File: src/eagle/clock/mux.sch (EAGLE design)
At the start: 52 parts, among them U1 SN74HC595N, U2 SN74HC595N, U3 SN74HC595N

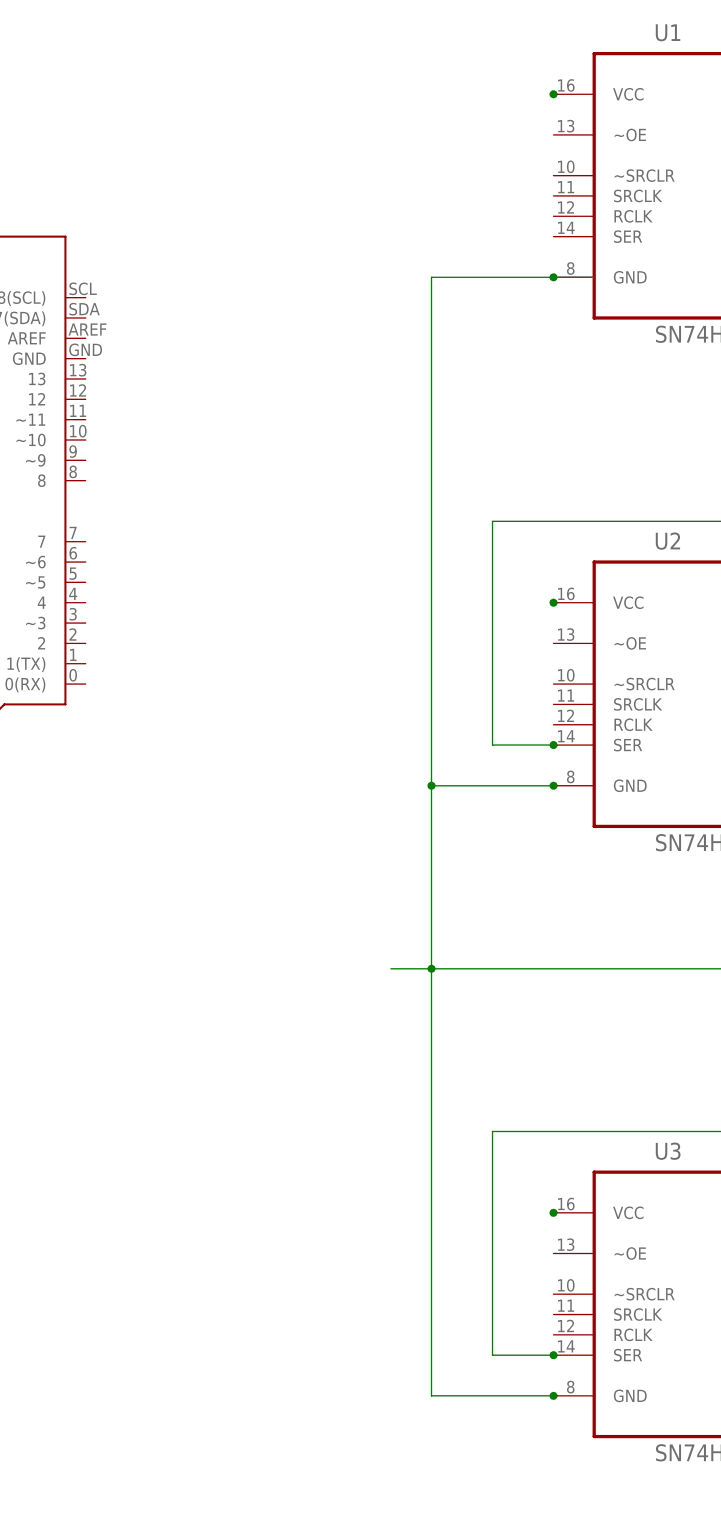
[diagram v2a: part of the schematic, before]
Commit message: Connect ~OE to GND
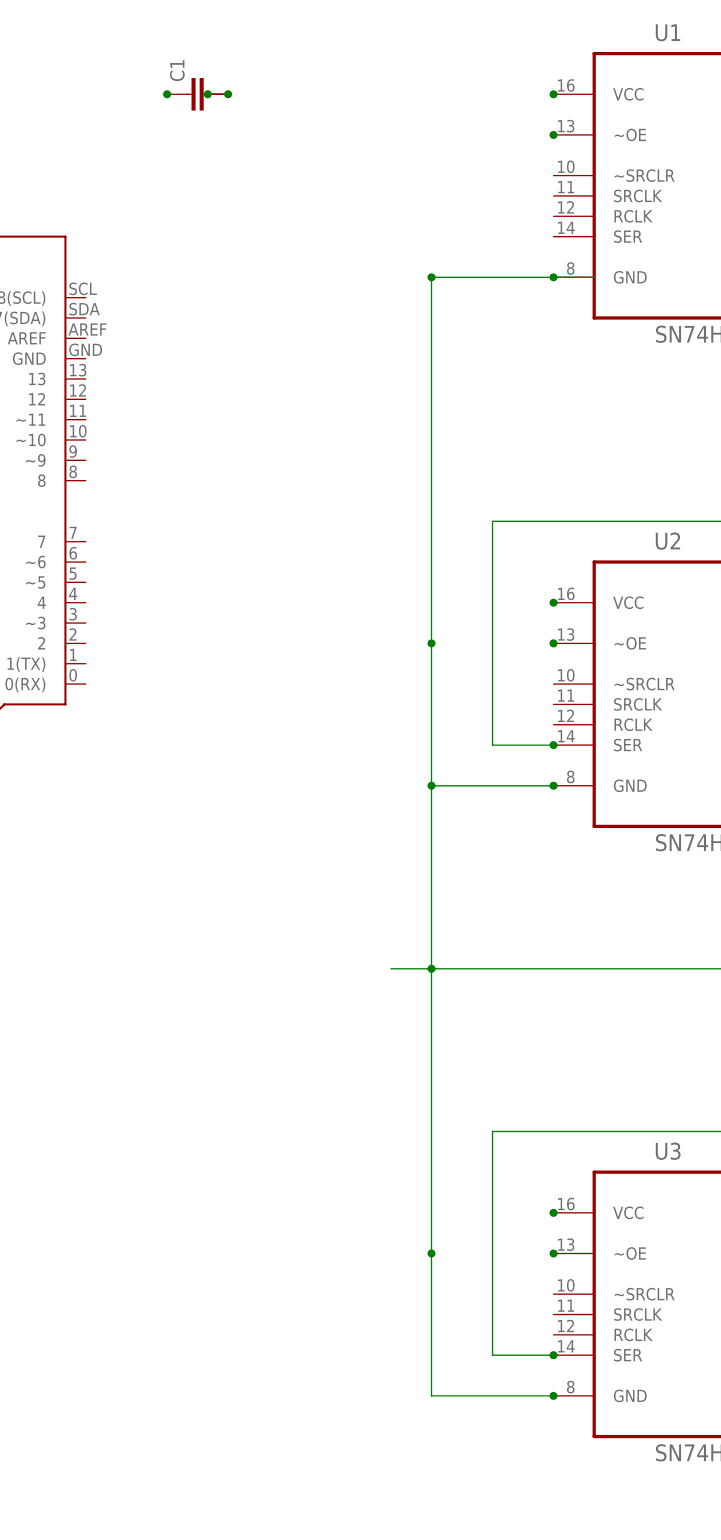
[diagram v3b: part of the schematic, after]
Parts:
- added C1: (no value), capacitor-wima:C-10-15/6
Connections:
- new net N$50: C1.1
- new net N$51: C1.2
- new net N$59: C1.3
- new net N$60: U1.~OE
- new net N$61: U2.~OE
- new net N$62: U3.~OE
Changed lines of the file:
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@@
 <part name="U3" library="SN74HC595N" deviceset="SN74HC595N" device=""/>
 <part name="PCB1" library="E14_Arduino_published" deviceset="ARDUINO_UNO" device=""/>
+<part name="C1" library="capacitor-wima" deviceset="C-" device="10-15/6"/>
 </parts>
 <sheets>
@@
 <plain>
 <wire x1="20.32" y1="60.96" x2="-7.62" y2="60.96" width="0.1524" layer="93"/>
-<wire x1="-7.62" y1="60.96" x2="-116.84" y2="60.96" width="0.1524" layer="93"/>
 <wire x1="-7.62" y1="60.96" x2="-7.62" y2="-2.54" width="0.1524" layer="93"/>
 <wire x1="-7.62" y1="-2.54" x2="20.32" y2="-2.54" width="0.1524" layer="93"/>
@@
 <wire x1="-116.84" y1="60.96" x2="-116.84" y2="15.24" width="0.1524" layer="93"/>
 <wire x1="-116.84" y1="15.24" x2="-81.28" y2="15.24" width="0.1524" layer="93"/>
+<wire x1="-116.84" y1="60.96" x2="-7.62" y2="60.96" width="0.1524" layer="93"/>
+<wire x1="20.32" y1="55.88" x2="5.08" y2="55.88" width="0.1524" layer="93"/>
+<wire x1="5.08" y1="55.88" x2="5.08" y2="38.1" width="0.1524" layer="93"/>
+<wire x1="20.32" y1="-7.62" x2="5.08" y2="-7.62" width="0.1524" layer="93"/>
+<wire x1="20.32" y1="-83.82" x2="5.08" y2="-83.82" width="0.1524" layer="93"/>
 </plain>
 <instances>
@@
 <instance part="U3" gate="A" x="38.1" y="-86.36"/>
 <instance part="PCB1" gate="G$1" x="-58.42" y="12.7" rot="R270"/>
+<instance part="C1" gate="G$1" x="-25.4" y="60.96" rot="R90"/>
 </instances>
 <busses>
@@
 <wire x1="25.4" y1="38.1" x2="20.32" y2="38.1" width="0.1524" layer="91"/>
 <wire x1="20.32" y1="38.1" x2="5.08" y2="38.1" width="0.1524" layer="91"/>
-<wire x1="5.08" y1="38.1" x2="5.08" y2="-25.4" width="0.1524" layer="91"/>
+<wire x1="5.08" y1="38.1" x2="5.08" y2="-7.62" width="0.1524" layer="91"/>
 <pinref part="U2" gate="A" pin="GND"/>
+<wire x1="5.08" y1="-7.62" x2="5.08" y2="-25.4" width="0.1524" layer="91"/>
 <wire x1="5.08" y1="-25.4" x2="20.32" y2="-25.4" width="0.1524" layer="91"/>
 <wire x1="5.08" y1="-25.4" x2="5.08" y2="-48.26" width="0.1524" layer="91"/>
 <pinref part="U3" gate="A" pin="GND"/>
-<wire x1="5.08" y1="-48.26" x2="5.08" y2="-101.6" width="0.1524" layer="91"/>
+<wire x1="5.08" y1="-48.26" x2="5.08" y2="-83.82" width="0.1524" layer="91"/>
+<wire x1="5.08" y1="-83.82" x2="5.08" y2="-101.6" width="0.1524" layer="91"/>
 <wire x1="5.08" y1="-101.6" x2="20.32" y2="-101.6" width="0.1524" layer="91"/>
 <pinref part="U1" gate="A" pin="GND"/>
@@
 <junction x="5.08" y="-48.26"/>
 <junction x="5.08" y="-25.4"/>
+<junction x="5.08" y="-83.82"/>
+<junction x="5.08" y="-7.62"/>
+<junction x="5.08" y="38.1"/>
 </segment>
 </net>
@@
 </segment>
 </net>
+<net name="N$50" class="0">
+<segment>
+<pinref part="C1" gate="G$1" pin="1"/>
+<junction x="-27.94" y="60.96"/>
+</segment>
+</net>
+<net name="N$51" class="0">
+<segment>
+<pinref part="C1" gate="G$1" pin="2"/>
+<junction x="-20.32" y="60.96"/>
+</segment>
+</net>
+<net name="N$59" class="0">
+<segment>
+<pinref part="C1" gate="G$1" pin="3"/>
+<junction x="-22.86" y="60.96"/>
+</segment>
+</net>
+<net name="N$60" class="0">
+<segment>
+<pinref part="U1" gate="A" pin="~OE"/>
+<junction x="20.32" y="55.88"/>
+</segment>
+</net>
+<net name="N$61" class="0">
+<segment>
+<pinref part="U2" gate="A" pin="~OE"/>
+<junction x="20.32" y="-7.62"/>
+</segment>
+</net>
+<net name="N$62" class="0">
+<segment>
+<pinref part="U3" gate="A" pin="~OE"/>
+<junction x="20.32" y="-83.82"/>
+</segment>
+</net>

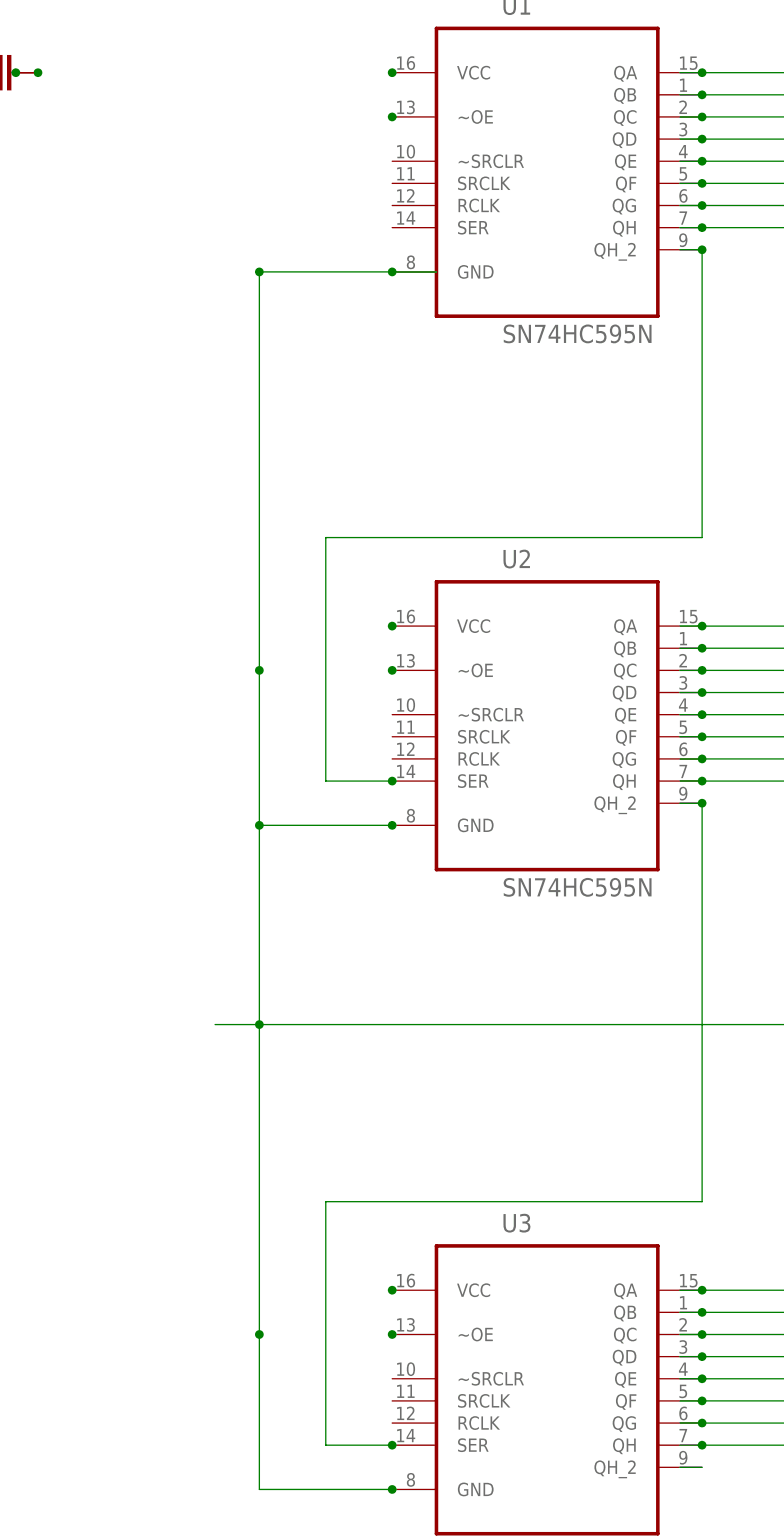
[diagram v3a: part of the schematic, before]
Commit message: 5V=>~SRCLR
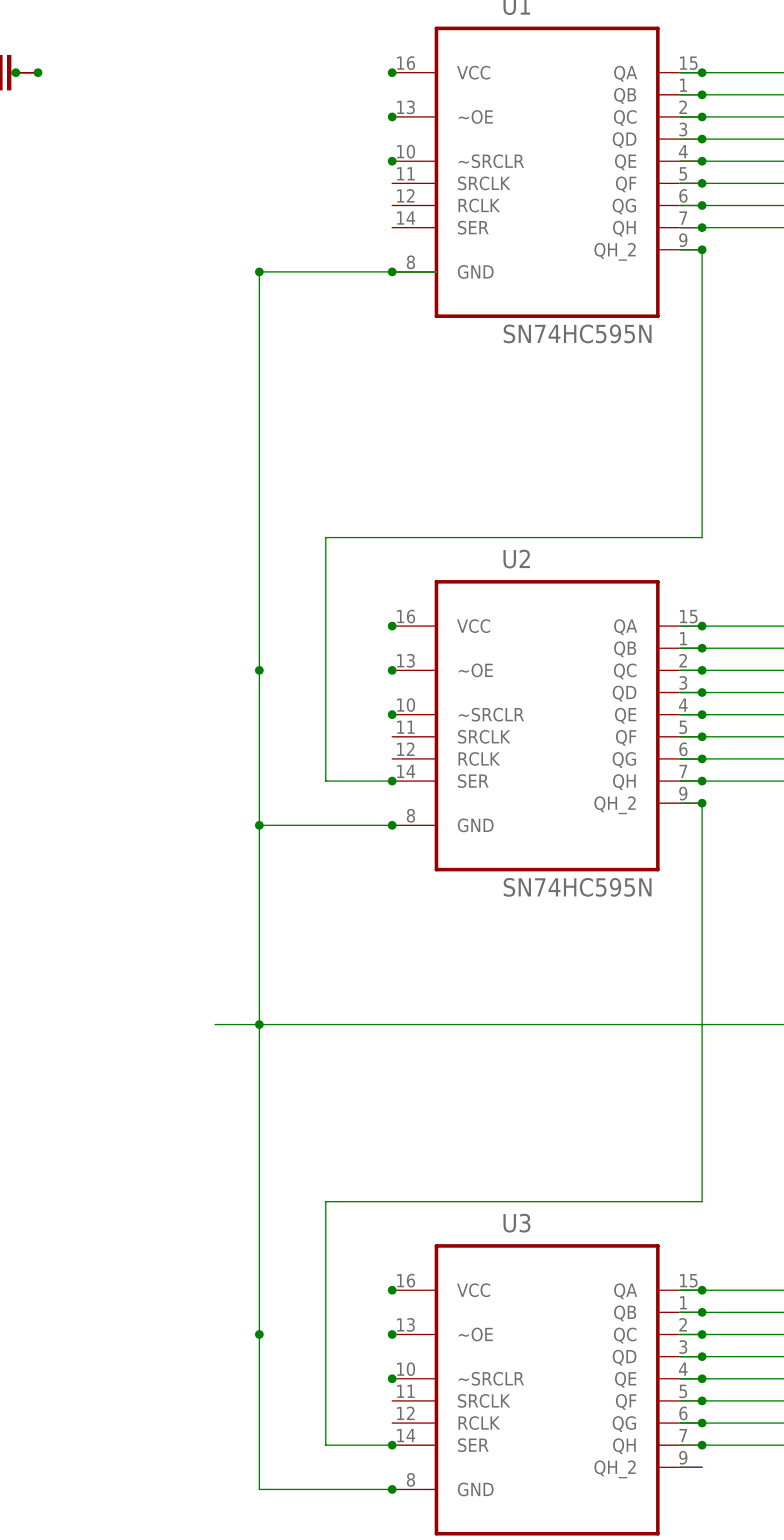
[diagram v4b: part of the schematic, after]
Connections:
- new net N$63: U3.~SRCLR
- new net N$64: U2.~SRCLR
- new net N$65: U1.~SRCLR
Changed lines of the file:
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@@
 <plain>
 <wire x1="20.32" y1="60.96" x2="-7.62" y2="60.96" width="0.1524" layer="93"/>
-<wire x1="-7.62" y1="60.96" x2="-7.62" y2="-2.54" width="0.1524" layer="93"/>
+<wire x1="-7.62" y1="60.96" x2="-7.62" y2="50.8" width="0.1524" layer="93"/>
+<wire x1="-7.62" y1="50.8" x2="-7.62" y2="-2.54" width="0.1524" layer="93"/>
 <wire x1="-7.62" y1="-2.54" x2="20.32" y2="-2.54" width="0.1524" layer="93"/>
 <wire x1="0" y1="-48.26" x2="-116.84" y2="-48.26" width="0.1524" layer="93"/>
 <wire x1="-116.84" y1="-48.26" x2="-116.84" y2="10.16" width="0.1524" layer="93"/>
 <wire x1="-116.84" y1="10.16" x2="-81.28" y2="10.16" width="0.1524" layer="93"/>
-<wire x1="-7.62" y1="-2.54" x2="-7.62" y2="-78.74" width="0.1524" layer="93"/>
-<wire x1="-7.62" y1="-78.74" x2="20.32" y2="-78.74" width="0.1524" layer="93"/>
+<wire x1="-7.62" y1="-2.54" x2="-7.62" y2="-12.7" width="0.1524" layer="93"/>
+<wire x1="-7.62" y1="-12.7" x2="-7.62" y2="-78.74" width="0.1524" layer="93"/>
+<wire x1="-7.62" y1="-78.74" x2="-7.62" y2="-88.9" width="0.1524" layer="93"/>
 <wire x1="-116.84" y1="60.96" x2="-116.84" y2="15.24" width="0.1524" layer="93"/>
 <wire x1="-116.84" y1="15.24" x2="-81.28" y2="15.24" width="0.1524" layer="93"/>
@@
 <wire x1="20.32" y1="-7.62" x2="5.08" y2="-7.62" width="0.1524" layer="93"/>
 <wire x1="20.32" y1="-83.82" x2="5.08" y2="-83.82" width="0.1524" layer="93"/>
+<wire x1="20.32" y1="50.8" x2="-7.62" y2="50.8" width="0.1524" layer="93"/>
+<wire x1="20.32" y1="-12.7" x2="-7.62" y2="-12.7" width="0.1524" layer="93"/>
+<wire x1="20.32" y1="-88.9" x2="-7.62" y2="-88.9" width="0.1524" layer="93"/>
+<wire x1="-7.62" y1="-78.74" x2="20.32" y2="-78.74" width="0.1524" layer="93"/>
 </plain>
 <instances>
@@
 </segment>
 </net>
+<net name="N$63" class="0">
+<segment>
+<pinref part="U3" gate="A" pin="~SRCLR"/>
+<junction x="20.32" y="-88.9"/>
+</segment>
+</net>
+<net name="N$64" class="0">
+<segment>
+<pinref part="U2" gate="A" pin="~SRCLR"/>
+<junction x="20.32" y="-12.7"/>
+</segment>
+</net>
+<net name="N$65" class="0">
+<segment>
+<pinref part="U1" gate="A" pin="~SRCLR"/>
+<junction x="20.32" y="50.8"/>
+</segment>
+</net>
